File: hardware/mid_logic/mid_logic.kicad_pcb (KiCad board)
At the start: 4 copper layers, 52 x 52 mm, 48 parts, among them J2 J_STK_A, J3 J_STK_B, J4 RS485 A/B/GND, J5 Feld: 4 Reed, J6 Haubenkontakt, Q2 BC847, SW1 RESET, SW2 BOOT, U1 ESP32-S3-WROOM-1-N16R8, U2 MAX3485, U3 PCF8575, U4 PhotoMOS 60V

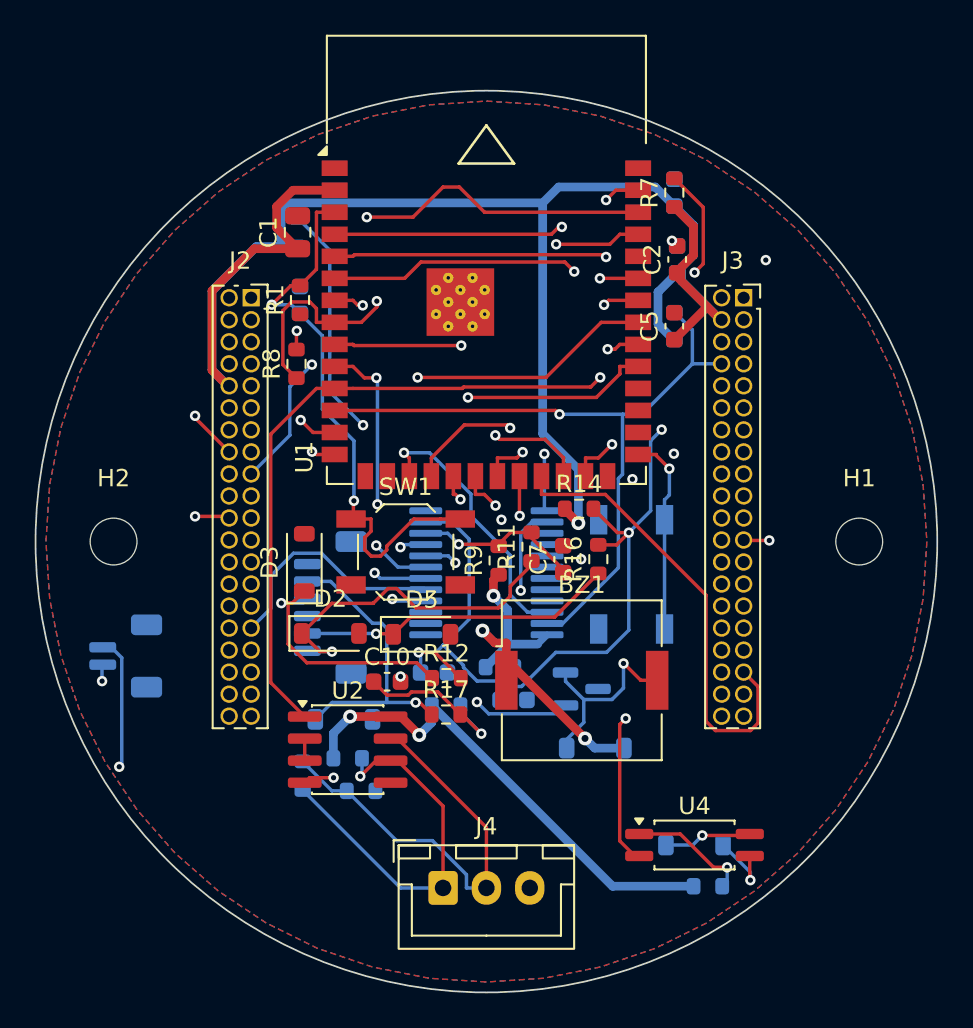
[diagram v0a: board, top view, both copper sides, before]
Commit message: USB-C wandert auf das Mid-Board, Top bekommt eine Randkerbe
Der Grund ist Bauhoehe, nicht Routing. Ueber dem Top-Board sind bis zur
Zentralscheibe 3,5 mm frei; eine stehende USB-C-Buchse baut 7 bis 9,25 mm
(GCT USB4115: H = 9,25 mm laut Datenblatt). Sie haette die Scheibe
durchstossen. Zwischen Mids und Tops Oberseite liegen dagegen 10,0 mm.

Die Buchse steht jetzt auf Mid bei (3,5 / 20,3) und greift durch eine offene
Randkerbe des Top-Boards nach vorn - gesteckt wird weiterhin frontal, sobald
die Zentralscheibe ab ist. Koerper 8,3 x 4,3 mm, Kerbe 11,0 mm breit ab
y = 16,8 bis zum Rand.

Offene Kerbe statt Fenster, weil der Boardrand bei y = 23,5 liegt: Ein
geschlossenes Fenster liesse einen Steg von einem halben Millimeter stehen,
der beim Nutzentrennen bricht.

MITGEWANDERT sind die ESD-Diode (U5) und die beiden CC-Widerstaende
(R18/R19). Damit verlieren USB_DP und USB_DN ihren Weg durch den Stapel:
J_STK_A 34/36 heissen jetzt RSV_A3/RSV_A5. Der native USB des ESP32-S3 sitzt
auf demselben Board wie die Buchse. Stack-Pinout auf v0.4.

USB_VBUS bleibt auf A18 - es geht weiter nach unten zum Power-Mux auf Bottom,
kommt jetzt nur von Mid statt von Top.

PLATZIERUNG. Der Bodenrand von Mid war belegt: RS485 (J4) nach links auf
(-11,5 / 19,0) gerueckt, PhotoMOS (U4) aus der Fixliste genommen. Ein
Rastersuchlauf ueber beide Seiten fand fuer U4 keine freie Flaeche von
11,6 x 3,6 mm - der automatische Platzierer bringt ihn jetzt selbst unter und
hat ihn nach (-20,1 / 7,9) gelegt. Oben ging es nicht, dort steht das
ESP32-Modul mit seiner Antenne; links und rechts laesst Tops Displayfenster
nur 7,2 mm Rand.

inside_outline() kennt die Kerbe, der Platzierer legt dort nichts ab, und der
Zonenumriss folgt ihr.

  top_ui     27 -> 21 Bauteile, unrouted 63 -> 48
  mid_logic  46 -> 50 Bauteile

Co-Authored-By: Claude Opus 5 (1M context) <noreply@anthropic.com>
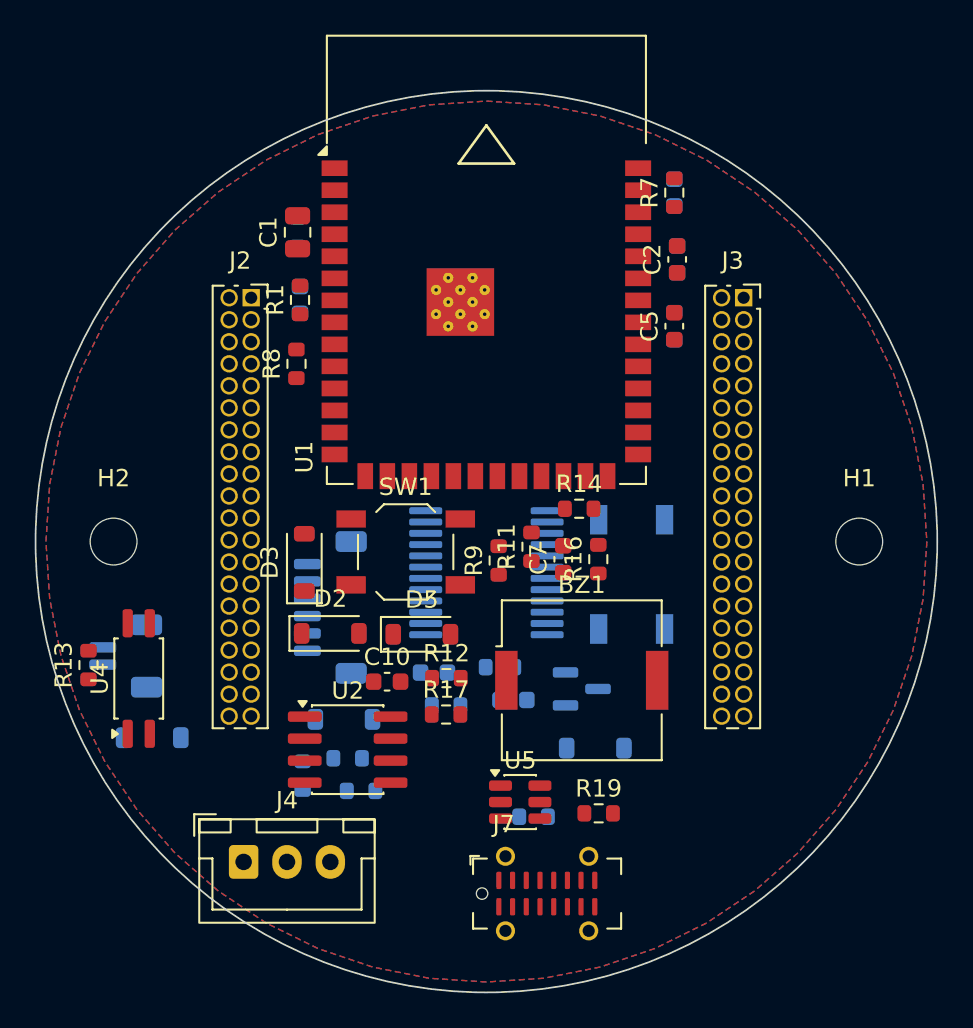
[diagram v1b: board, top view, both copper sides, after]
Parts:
- added J7: USB-C, USB_C_Receptacle_G-Switch_GT-USB-7051x, F.Cu at (3.50, 20.3)
- added R18: 5k1, R_0603_1608Metric, B.Cu at (2.72, 15.9)
- added R19: 5k1, R_0603_1608Metric, F.Cu at (6.47, 15.7)
- added U5: USBLC6-2SC6, SOT-23-6, F.Cu at (1.95, 15.0)
- R13: moved to F.Cu
- moved R13 37.9 mm to (-22.9, 7.12), turned to 90 degrees
- moved U4 33.5 mm to (-20.1, 7.90), turned to 90 degrees
- moved D4 31.9 mm to (-19.3, 11.3)
- moved J4 11.6 mm to (-14.0, 18.5)
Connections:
- J2 pad 34: USB_DP -> RSV_A3
- J2 pad 36: USB_DN -> RSV_A5
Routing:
- net 3V3_SYS: track 177.4 -> 0.00 mm, vias 4 -> 0
- net AUDIO_PWM: track 53.8 -> 0.00 mm, vias 3 -> 0
- net I2C_SCL: track 53.4 -> 0.00 mm, vias 2 -> 0
- net UART485_TX: track 51.4 -> 0.00 mm, vias 3 -> 0
- net HOOD_B: track 50.9 -> 0.00 mm, vias 2 -> 0
- net M2_INB: track 50.4 -> 0.00 mm, vias 2 -> 0
- net BTN4: track 46.8 -> 0.00 mm, vias 1 -> 0
- net M1_INA: track 46.4 -> 0.00 mm, vias 2 -> 0
- net UART485_RX: track 45.7 -> 0.00 mm, vias 1 -> 0
- net I_SENSE2: track 45.4 -> 0.00 mm, vias 1 -> 0
- net HOOD_A: track 44.7 -> 0.00 mm, vias 2 -> 0
- net ESP_BOOT: track 43.8 -> 0.00 mm, vias 2 -> 0
- net I_SENSE1: track 43.0 -> 0.00 mm, vias 1 -> 0
- net BTN2: track 42.7 -> 0.00 mm, vias 1 -> 0
- net I2C_SDA: track 41.4 -> 0.00 mm, vias 1 -> 0
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
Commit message: Stack-Pinout v0.5: Tasten und I2C auf die Aussenreihe, Tasten auf beide Verbinder
Zwei Autorouter (1.9.0 und 2.3.0) und zwei Lagenzahlen hatten auf Top exakt
dieselben elf offenen Netze hinterlassen. Das ist kein Werkzeugproblem,
sondern die Pinbelegung.

BTN1..BTN4 lagen auf B26..B29 - vier benachbarten Kontakten der INNENreihe
des RECHTEN Verbinders. Ihre Taster sitzen aber in allen vier Ecken des
Top-Boards, zwei davon links. Zwei Bahnen mussten quer ueber ein Board mit
80 Steckkontakten im 1,27-mm-Raster, und alle vier zuerst aus der Innenreihe
heraus. I2C_SCL/SDA lagen ebenfalls innen.

Neu liegt jedes Tastennetz auf der AUSSENreihe des Verbinders, der seiner
Ecke am naechsten ist - von dort geht es direkt nach aussen und am Boardrand
entlang zum Taster:

  BTN1  B26 -> B1    aussen, y = -14,06   SW1 (+18 / -20)
  BTN2  B27 -> A2    aussen, y = -14,06   SW2 (-18 / -20)
  BTN3  B28 -> A40   aussen, y = +10,07   SW3 (-18 / +20)
  BTN4  B29 -> B39   aussen, y = +10,07   SW4 (+18 / +20)

  I2C_SCL  B6 -> B5  aussen
  I2C_SDA  B8 -> B7  aussen

Beide I2C-Teilnehmer auf Top - SHT4x und ToF - sitzen an der oberen Kante,
also dort, wo die neuen Pins liegen.

Die freigewordenen Kontakte B6, B8, B26..B29 werden PGND. Vier PGND-Pins sind
weggefallen (A2, A40, B1, B39); ueber beide Verbinder bleiben 25.

Alle drei Schaltplaene und Layouts neu erzeugt, Netzlistenvergleich bestanden,
keine Platzierungsfehler. Das Routing folgt.

Co-Authored-By: Claude Opus 5 (1M context) <noreply@anthropic.com>
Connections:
- J2 pad 2: PGND -> BTN2
- J2 pad 40: PGND -> BTN3
- J3 pad 1: PGND -> BTN1
- J3 pad 26: BTN1 -> PGND
- J3 pad 27: BTN2 -> PGND
- J3 pad 28: BTN3 -> PGND
- J3 pad 29: BTN4 -> PGND
- J3 pad 39: PGND -> BTN4
- J3 pad 5: PGND -> I2C_SCL
- J3 pad 6: I2C_SCL -> PGND
- J3 pad 7: PGND -> I2C_SDA
- J3 pad 8: I2C_SDA -> PGND

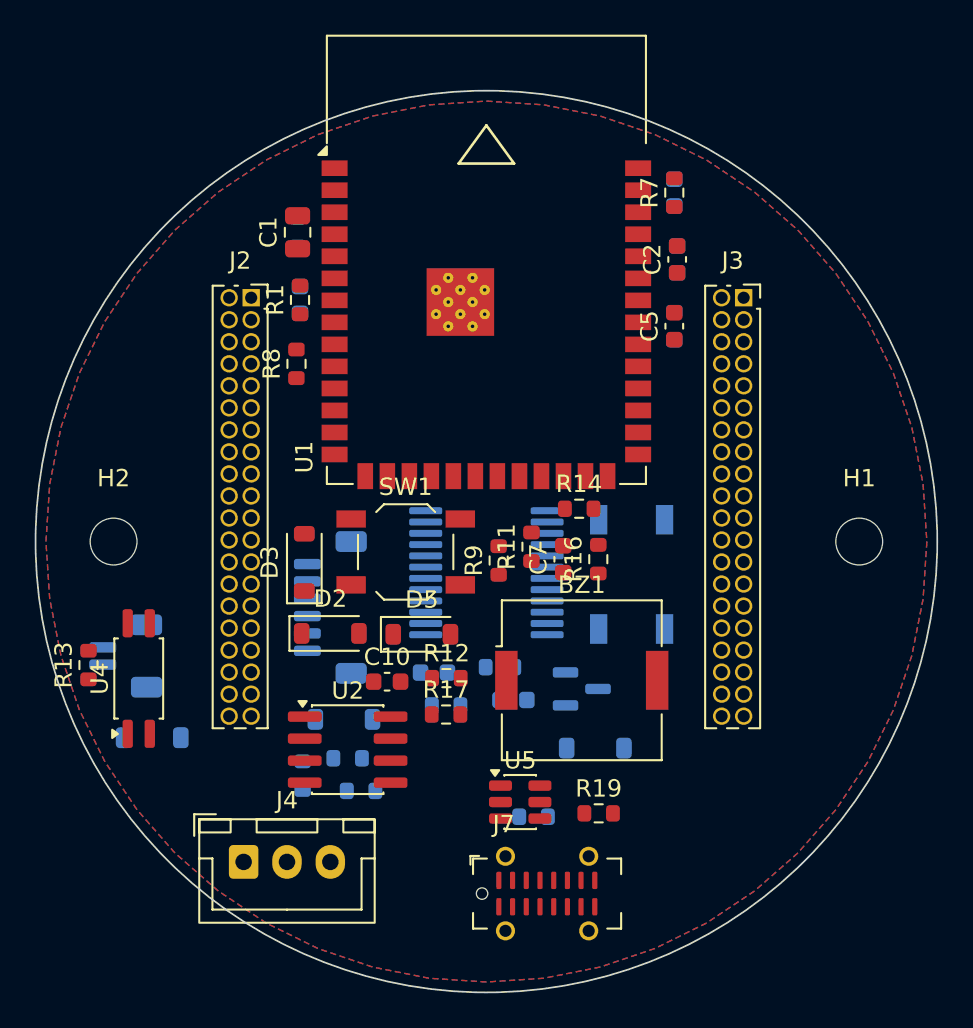
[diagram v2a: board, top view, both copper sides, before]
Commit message: Quadratischer Randkeepout: Top faellt von 11 auf 3 offene Netze
Der Kreisring war die Wand. Mit vier Balken entlang der Kanten statt eines
Annulus routet Freerouting auf Top durch:

              Segmente  Vias  offene Signale
  vorher         144      9        11
  jetzt          175     15         3   (3V3_SYS, I2C_SCL, I2C_SDA)

Alle vier Tastennetze und alle vier Stern-Netze sind jetzt verbunden. Damit
ist auch rueckwirkend klar, dass weder die Lagenzahl noch der Routerwechsel
noch das neue Pinout je eine Chance hatten - sie haben alle gegen dieselbe
unsichtbare Sperre gearbeitet.

DIE PROJEKTDATEIEN WERDEN BEIM SPEICHERN ZURUECKGESETZT. pcbnew.SaveBoard
legt die .kicad_pro mit KiCads Vorgaben neu an; die bewussten Entscheidungen
von gestern - 0,15 mm Abstand statt 0,2, ein Waermefallensteg statt zwei -
waren dadurch beim Neuerzeugen still verschwunden und erzeugten prompt wieder
Scheinverletzungen (Bottom 2 clearance, alle drei zusammen 34
starved_thermal). BoardBuilder.save() schreibt sie jetzt nach jedem Speichern
zurueck.

  starved_thermal  34 -> 0
  clearance         2 -> 1

STAND NACH gnd_connect

                Segmente  offene Signale  Masse-Inseln  Kupferfehler
  top_ui           175          3              1             1
  mid_logic        641          9             12             0
  bottom_power    1430          4             26             1

Der eine Kupferfehler auf Top ist der dokumentierte, absichtliche Ueberhang
der Klinkenbuchse ueber die Boardkante; der auf Bottom ein Haarriss von
0,1 statt 0,15 mm zwischen zwei Leistungsbahnen.

Co-Authored-By: Claude Opus 5 (1M context) <noreply@anthropic.com>
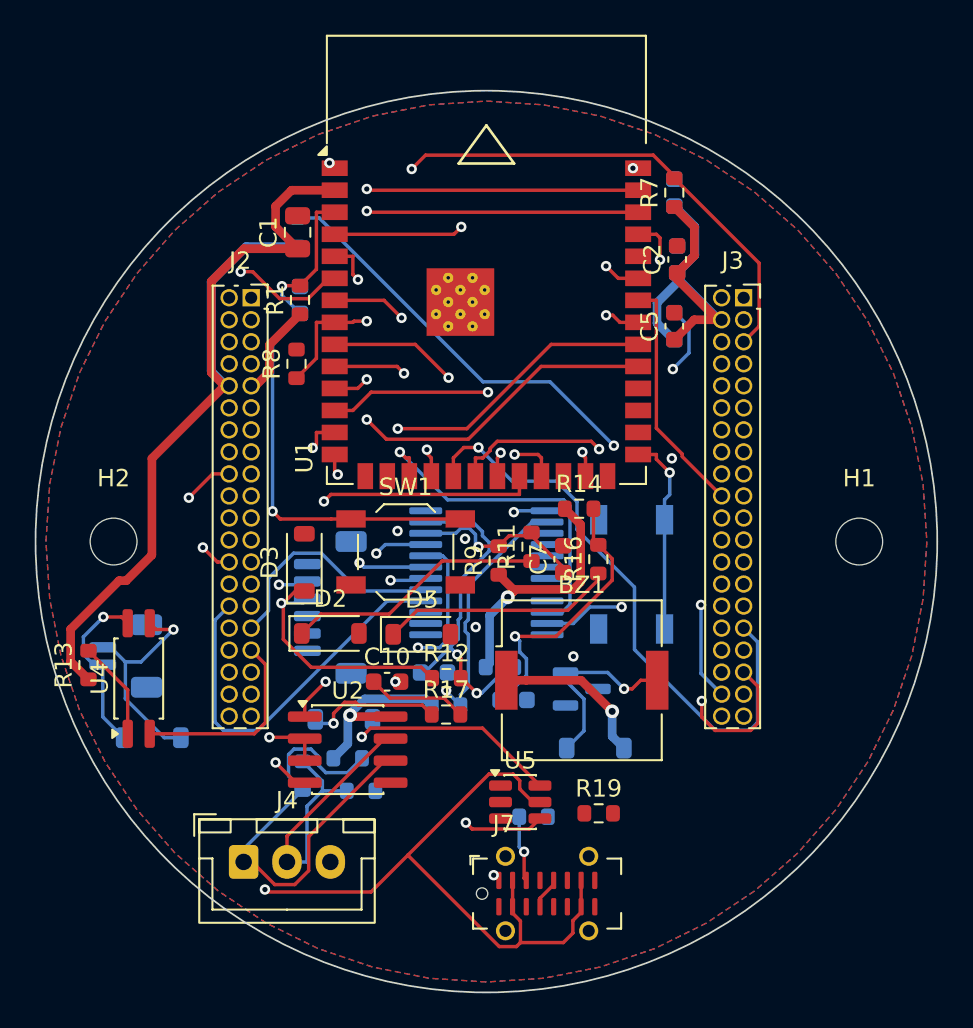
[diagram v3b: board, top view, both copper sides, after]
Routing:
- net 3V3_SYS: track 0.00 -> 177.2 mm, vias 0 -> 2
- net I2C_SCL: track 0.00 -> 67.1 mm, vias 0 -> 2
- net USB_VBUS: track 0.00 -> 66.0 mm, vias 0 -> 2
- net I2C_SDA: track 0.00 -> 63.9 mm, vias 0 -> 3
- net AUDIO_PWM: track 0.00 -> 54.2 mm, vias 0 -> 1
- net UART485_TX: track 0.00 -> 53.9 mm, vias 0 -> 3
- net I_SENSE2: track 0.00 -> 44.6 mm, vias 0 -> 1
- net I_SENSE1: track 0.00 -> 44.6 mm, vias 0 -> 2
- net 5V_SYS: track 0.00 -> 44.1 mm, vias 0 -> 1
- net RS485_DIR: track 0.00 -> 43.2 mm, vias 0 -> 2
- net UART485_RX: track 0.00 -> 43.0 mm, vias 0 -> 2
- net PRESENCE_INT: track 0.00 -> 41.8 mm, vias 0 -> 1
- net M1_INA: track 0.00 -> 40.7 mm, vias 0 -> 1
- net QSPI_D2: track 0.00 -> 39.7 mm, vias 0 -> 3
- net DISP_RST: track 0.00 -> 39.4 mm, vias 0 -> 1
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
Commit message: Der Original-Controller bestaetigt die Strommessung ein viertes Mal
Der mitgelieferte K0000230 lag offen auf dem Tisch. Drei Bauteile darauf
sagen dasselbe wie unsere drei Messungen - und man muss dafuer nichts messen:

  Shunt 50 mOhm je Kanal   bei 1,7 A sind das 85 mV und 0,14 W.
                           Bei 20 A waeren es 20 WATT in einem Chipwiderstand.
  2x Infineon BTM7700G     integrierte H-Bruecke, rund 110 mOhm im Strompfad.
                           Bei 1,7 A 0,32 W, bei 20 A 44 W in einem SO-28.
  Elko 47 uF               fuer zwei Motoren. Wer 20-A-Impulse abfaengt,
                           baut Hunderte von Mikrofarad ein.

Drei unabhaengige Bauteilentscheidungen, alle nur mit ein bis zwei Ampere
vereinbar. docs/14 neu, mit der vollstaendigen Bauteilliste.

DREI FOLGERUNGEN FUER UNS

1) Unsere diskrete Bruecke aus acht MOSFETs und vier Gate-Treibern loest der
   Hersteller mit ZWEI ICs. Das war Punkt 55; das Argument dagegen (Platine
   ist geroutet) steht weiter, aber die Sachlage ist jetzt belegt statt
   vermutet. Der BTM7700G selbst waere fuer uns grenzwertig - seine
   Kurzschlussfestigkeit endet bei 28 V, unsere Schiene liegt bei 26,4 V.

2) Der Bulk-Kondensator darf schrumpfen. docs/01 sieht 470 bis 1000 uF vor,
   das Original kommt mit 47 uF aus. Das ist die praktisch wertvollste
   Erkenntnis, denn der Elko ist eines der groessten Teile auf der Kabelseite
   von Bottom - genau dort, wo heute der Platz fuer einen zusammengefassten
   Feldstecker fehlt. Nicht blind uebernehmen: 100 bis 220 uF sind die
   naheliegende Groessenordnung fuer unsere PWM-Topologie.

3) Der Hersteller trennt seine Eingaenge galvanisch (zwei Optokoppler), wir
   nicht. Bei reiner SELV-Verkabelung zulaessig, aber ein Konzeptunterschied.

Ausserdem in diesem Commit:

  3D-Modelle fuer die drei Steckverbinder, die KiCad nicht mitliefert
  (mechanical/connector_models.py) - Huellkoerper aus dem F.Fab-Grundriss,
  Hoehen mit Quelle dokumentiert. gen_layouts haengt sie 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
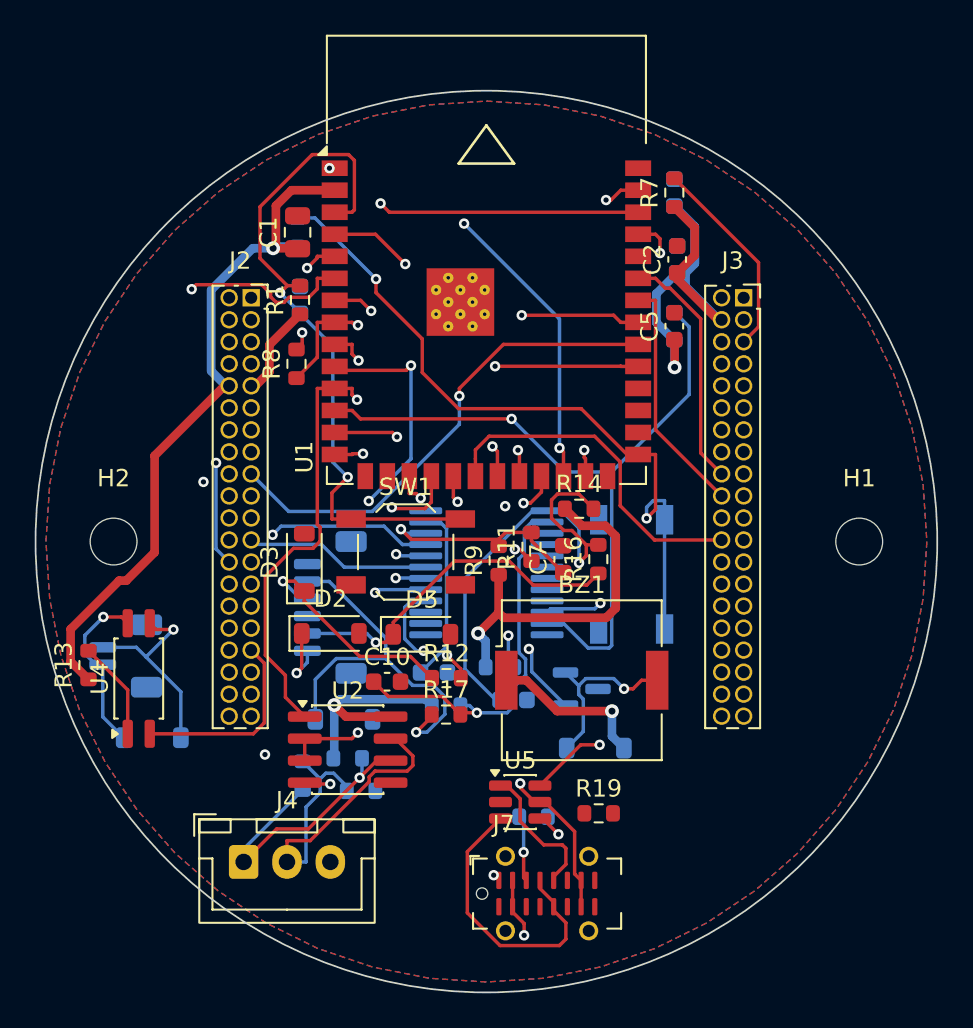
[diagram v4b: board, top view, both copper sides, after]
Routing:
- net M2_INB: track 0.00 -> 47.1 mm, vias 0 -> 3
- net AUDIO_B: track 0.00 -> 30.0 mm, vias 0 -> 2
- net QSPI_D2: track 39.7 -> 18.1 mm, vias 3 -> 1
- net REED1_IN: track 15.0 -> 36.1 mm, vias 0 -> 3
- net USB_DP_C: track 0.00 -> 16.9 mm
- net 3V3_SYS: track 177.2 -> 166.5 mm, vias 2 -> 4
- net RS485_A: track 26.6 -> 17.6 mm, vias 0 -> 1
- net ESP_EN: track 31.8 -> 39.8 mm
- net USB_VBUS: track 66.0 -> 58.3 mm
- net SAB1_IN: track 13.5 -> 20.2 mm, vias 0 -> 1
- net USB_DN_C: track 1.85 -> 8.17 mm
- net I2C_SDA: track 63.9 -> 69.8 mm, vias 3 -> 1
- net AUDIO_PWM: track 54.2 -> 48.5 mm
- net HW_TRIP1: track 22.5 -> 26.5 mm, vias 0 -> 1
- net UART_AUX_TX: track 18.0 -> 14.0 mm, vias 2 -> 0
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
